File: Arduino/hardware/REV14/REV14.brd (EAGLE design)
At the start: 100 x 50 mm, 57 parts, among them IC1 LTC3525, IC2 ATMEGA168-AU, IC3 TS1003IG5TMF, Q1 32768Hz, U1 RN2483, U2 TMP112

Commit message: rev 14 really ready now
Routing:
- net SCL: track 95.6 -> 90.3 mm
- net GND: vias 128 -> 131
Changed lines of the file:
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@@
 <via x="95.09" y="25.175" extent="1-16" drill="0.5"/>
 <via x="63.6575" y="29.62" extent="1-16" drill="0.5"/>
+<via x="24.2875" y="29.62" extent="1-16" drill="0.5"/>
+<via x="29.3675" y="23.27" extent="1-16" drill="0.5"/>
+<via x="31.59" y="13.745" extent="1-16" drill="0.5"/>
 </signal>
 <signal name="VCC" class="1">
@@
 <wire x1="57.39" y1="31.75" x2="55.88" y2="31.75" width="0.2032" layer="1"/>
 <wire x1="55.88" y1="31.75" x2="55.88" y2="28.125" width="0.2032" layer="1"/>
-<wire x1="55.88" y1="28.125" x2="55.88" y2="27.7175" width="0.2032" layer="1"/>
-<wire x1="55.88" y1="27.7175" x2="57.88" y2="25.7175" width="0.2032" layer="1" curve="90"/>
-<wire x1="57.88" y1="25.7175" x2="60.0075" y2="25.7175" width="0.2032" layer="1"/>
 <wire x1="57.42" y1="31.78" x2="57.42" y2="32.4325" width="0.2032" layer="1"/>
 <wire x1="57.42" y1="32.4325" x2="57.15" y2="32.7025" width="0.2032" layer="1" curve="90"/>
@@
 <contactref element="TP1" pad="TP"/>
 <wire x1="22.0025" y1="48.895" x2="18.7325" y2="45.9425" width="1.016" layer="1" curve="90"/>
-<wire x1="18.7325" y1="45.9425" x2="18.7325" y2="44.2275" width="1.016" layer="1"/>
+<wire x1="18.7325" y1="45.9425" x2="18.7325" y2="45.75" width="1.016" layer="1"/>
+<wire x1="18.7325" y1="45.75" x2="18.7325" y2="45.72" width="1.016" layer="1"/>
+<wire x1="18.7325" y1="45.72" x2="18.7325" y2="44.2275" width="1.016" layer="1"/>
 <wire x1="18.7325" y1="44.2275" x2="18.5975" y2="44.2275" width="0.4064" layer="1"/>
 <wire x1="22.0025" y1="48.895" x2="93.000815625" y2="48.895" width="1.016" layer="1"/>
 <contactref element="PAD3" pad="1"/>
-<wire x1="18.7325" y1="45.9425" x2="18.7325" y2="45.72" width="0" layer="19" extent="1-1"/>
+<wire x1="18.75" y1="45.75" x2="18.7325" y2="45.72" width="2.1844" layer="1"/>
+<wire x1="18.75" y1="45.75" x2="18.7325" y2="45.75" width="2.1844" layer="1"/>
 </signal>
 <signal name="N$33" class="2">
@@
 <wire x1="2.635" y1="48.895" x2="4.985" y2="48.895" width="1.016" layer="1"/>
 <wire x1="4.985" y1="48.895" x2="6.985" y2="45.9425" width="1.016" layer="1" curve="-90"/>
-<wire x1="6.985" y1="45.9425" x2="6.985" y2="44.2275" width="1.016" layer="1"/>
+<wire x1="6.985" y1="45.9425" x2="6.985" y2="45.75" width="1.016" layer="1"/>
+<wire x1="6.985" y1="45.75" x2="6.985" y2="45.72" width="1.016" layer="1"/>
+<wire x1="6.985" y1="45.72" x2="6.985" y2="44.2275" width="1.016" layer="1"/>
 <wire x1="6.985" y1="44.2275" x2="7.1475" y2="44.2275" width="0.4064" layer="1"/>
 <wire x1="2.9525" y1="0.97" x2="0.97" y2="2.9525" width="1.016" layer="1" curve="-90"/>
@@
 <contactref element="TP4" pad="TP"/>
 <wire x1="92.71" y1="0.97" x2="2.9525" y2="0.97" width="1.016" layer="1"/>
-<wire x1="6.985" y1="45.9425" x2="6.985" y2="45.72" width="0" layer="19" extent="1-1"/>
+<wire x1="7" y1="45.75" x2="6.985" y2="45.72" width="2.1844" layer="1"/>
+<wire x1="7" y1="45.75" x2="6.985" y2="45.75" width="2.1844" layer="1"/>
 </signal>
 <signal name="N$2">

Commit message: rev14 without blooper
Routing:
- net SCL: track 90.3 -> 88.7 mm
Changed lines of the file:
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@@
 <contactref element="FTDI_RN2483" pad="1"/>
 <via x="61.055" y="38.325" extent="1-16" drill="0.5"/>
-<wire x1="58.6025" y1="38.29" x2="61.055" y2="38.29" width="0.4064" layer="1"/>
+<wire x1="58.6025" y1="38.29" x2="61.055" y2="38.29" width="0.3048" layer="1"/>
 <wire x1="61.055" y1="38.29" x2="61.055" y2="38.325" width="0.4064" layer="1"/>
 <via x="58.1" y="34.515" extent="1-16" drill="0.5"/>
-<wire x1="58.1025" y1="36.64" x2="58.1" y2="36.64" width="0.4064" layer="1"/>
-<wire x1="58.1" y1="36.64" x2="58.1" y2="34.515" width="0.4064" layer="1"/>
+<wire x1="58.1025" y1="36.64" x2="58.1" y2="36.64" width="0.3048" layer="1"/>
+<wire x1="58.1" y1="36.64" x2="58.1" y2="34.515" width="0.3048" layer="1"/>
 <via x="38.5" y="24.765" extent="1-16" drill="0.5"/>
 <via x="39.935" y="28.8925" extent="1-16" drill="0.5"/>
@@
 <wire x1="57.365" y1="43.815" x2="57.5167125" y2="43.6632875" width="0.4064" layer="1"/>
 <wire x1="57.5167125" y1="43.6632875" x2="58.1025" y2="42.249071875" width="0.4064" layer="1" curve="-45.00009"/>
-<wire x1="58.1025" y1="42.249071875" x2="58.1025" y2="38.29" width="0.4064" layer="1"/>
+<wire x1="58.1025" y1="42.249071875" x2="58.1025" y2="38.29" width="0.3048" layer="1"/>
 <wire x1="54.2925" y1="38.315" x2="53.9257875" y2="38.6817125" width="0.4064" layer="1"/>
 <wire x1="53.9257875" y1="38.6817125" x2="53.34" y2="40.095928125" width="0.4064" layer="1" curve="-45.00009"/>
@@
 <contactref element="I2C_EXT" pad="11"/>
 <contactref element="U2" pad="6"/>
-<wire x1="57.6025" y1="38.29" x2="55.88" y2="38.29" width="0.2032" layer="1"/>
-<wire x1="55.88" y1="38.29" x2="55.88" y2="39.2425" width="0.2032" layer="1"/>
+<wire x1="57.6025" y1="38.29" x2="55.75" y2="38.29" width="0.2032" layer="1"/>
+<wire x1="55.75" y1="38.29" x2="55.75" y2="39.2425" width="0.2032" layer="1"/>
 <contactref element="JP2" pad="1"/>
-<wire x1="55.88" y1="39.2425" x2="55.88" y2="43.6" width="0.2032" layer="1"/>
-<wire x1="55.88" y1="43.6" x2="55.665" y2="43.815" width="0.4064" layer="1" curve="90"/>
+<wire x1="55.75" y1="39.2425" x2="55.75" y2="43.6" width="0.2032" layer="1"/>
+<wire x1="55.75" y1="43.6" x2="55.665" y2="43.815" width="0.4064" layer="1" curve="90"/>
 <contactref element="U$4" pad="1"/>
 <wire x1="57.42" y1="29.18" x2="59.295" y2="27.305" width="0.2032" layer="1" curve="90"/>
@@
 <wire x1="57.42" y1="29.18" x2="57.42" y2="27.575" width="0.2032" layer="1"/>
 <wire x1="57.42" y1="27.575" x2="57.15" y2="27.305" width="0.2032" layer="1" curve="-90"/>
-<wire x1="57.15" y1="27.305" x2="55.88" y2="27.305" width="0.2032" layer="16"/>
-<wire x1="55.88" y1="27.305" x2="55.88" y2="39.2425" width="0.2032" layer="16"/>
+<wire x1="57.15" y1="27.305" x2="55.75" y2="27.305" width="0.2032" layer="16"/>
+<wire x1="55.75" y1="27.305" x2="55.75" y2="39.2425" width="0.2032" layer="16"/>
 <via x="57.15" y="27.305" extent="1-16" drill="0.5"/>
-<via x="55.88" y="39.2425" extent="1-16" drill="0.5"/>
+<via x="55.75" y="39.2425" extent="1-16" drill="0.5"/>
 <wire x1="45" y1="25.375" x2="42.5" y2="25.375" width="0.2032" layer="1"/>
 <wire x1="46.375" y1="24" x2="45" y2="25.375" width="0.2032" layer="1"/>
@@
 <contactref element="I2C_EXT" pad="9"/>
 <contactref element="U2" pad="1"/>
-<wire x1="57.6025" y1="36.64" x2="56.515" y2="36.64" width="0.4064" layer="1"/>
+<wire x1="57.6025" y1="36.64" x2="56.515" y2="36.64" width="0.3048" layer="1"/>
 <contactref element="JP2" pad="2"/>
 <wire x1="56.515" y1="36.64" x2="55.88" y2="36.64" width="0.2032" layer="1"/>
 <wire x1="55.88" y1="36.64" x2="55.855" y2="36.615" width="0.2032" layer="1" curve="-90"/>
-<wire x1="55.855" y1="36.615" x2="55.7784" y2="36.615" width="0.2032" layer="1"/>
+<wire x1="55.855" y1="36.615" x2="55.75" y2="36.615" width="0.2032" layer="1"/>
 <contactref element="U$4" pad="6"/>
-<wire x1="55.7784" y1="36.615" x2="54.2925" y2="36.615" width="0.2032" layer="1"/>
+<wire x1="55.75" y1="36.615" x2="54.2925" y2="36.615" width="0.2032" layer="1"/>
 <wire x1="57.42" y1="31.78" x2="57.39" y2="31.75" width="0.4064" layer="1" curve="-90"/>
 <wire x1="57.39" y1="31.75" x2="55.88" y2="31.75" width="0.2032" layer="1"/>
@@
 <wire x1="86.25" y1="7.25" x2="86.36" y2="7.175" width="0.2032" layer="16"/>
 <wire x1="67.125" y1="42.75" x2="69.125" y2="42.75" width="0.2032" layer="1"/>
-<wire x1="59.895" y1="35.52" x2="61.0063" y2="36.6313" width="0.2032" layer="1"/>
 <wire x1="61.0063" y1="36.6313" x2="67.125" y2="42.75" width="0.2032" layer="1"/>
 <wire x1="69.125" y1="42.75" x2="69.215" y2="42.8625" width="0.2032" layer="1"/>
@@
 <wire x1="60.2488" y1="37.3888" x2="61.0063" y2="36.6313" width="0.2032" layer="1"/>
 <wire x1="55.9816" y1="37.3888" x2="60.2488" y2="37.3888" width="0.2032" layer="1"/>
-<wire x1="55.7784" y1="37.1856" x2="55.9816" y2="37.3888" width="0.2032" layer="1"/>
-<wire x1="55.7784" y1="36.615" x2="55.7784" y2="37.1856" width="0.2032" layer="1"/>
+<wire x1="55.75" y1="37.1856" x2="55.9816" y2="37.3888" width="0.2032" layer="1"/>
+<wire x1="55.75" y1="36.615" x2="55.75" y2="37.1856" width="0.2032" layer="1"/>
 </signal>
 <signal name="RESET">

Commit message: rev14 pre routing.... again :-D
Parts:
- removed PAD2, PAD3: (no value), wirepad:3,81/1,4
- removed TP4: TPSQTP06R, testpad:TP06R
- added TP3: TPSQTP07R, testpad:TP07R
- moved R17 19.4 mm to (36.5, 12.4)
- moved FTDI_RN2483 19.4 mm to (31.1, 7.30)
- moved R7 19.4 mm to (29.8, 11.1)
- moved C11 14.9 mm to (20.6, 7.30), turned to 0 degrees
- moved R5 8.86 mm to (16.8, 9.53), turned to 0 degrees
- moved PHT 8.03 mm to (44.5, 14.0)
- moved R1 8.03 mm to (43.2, 8.89)
- moved C5 3.19 mm to (94.3, 14.0)
- moved DQ 3.19 mm to (76.5, 13.3)
- moved R18 3.19 mm to (87.3, 15.2)
- moved R3 3.19 mm to (82.2, 15.2)
- moved R4 3.19 mm to (84.8, 15.2)
- moved R9 3.19 mm to (79.7, 15.2)
- moved I2C_EXT 3.19 mm to (85.4, 9.08)
- moved C3 2.25 mm to (97.5, 30.8)
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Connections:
- net N$22: no longer PAD3.1
- net N$33: now also TP3.TP; no longer PAD2.1, TP4.TP
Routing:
- net VCC: track 231.3 -> 96.8 mm
- net SPI_MOSI: track 90.1 -> 0.00 mm, vias 2 -> 0
- net PHONE: track 83.0 -> 0.00 mm, vias 5 -> 0
- net SPI_MISO: track 81.9 -> 0.00 mm, vias 3 -> 0
- net RFM_IRQ: track 74.2 -> 0.00 mm, vias 2 -> 0
- net SCL: track 88.7 -> 19.2 mm, vias 4 -> 2
- net SDA: track 95.8 -> 26.3 mm, vias 5 -> 2
- net SPI_SCK: track 66.7 -> 0.00 mm, vias 3 -> 0
- net RESET: track 66.7 -> 3.11 mm, vias 2 -> 0
- net D2: track 61.7 -> 0.00 mm
- net VCC1: track 63.1 -> 2.53 mm
- net IO_POWER_UP: track 60.3 -> 0.00 mm, vias 1 -> 0
- net SPI_NSS: track 55.9 -> 0.00 mm, vias 3 -> 0
- net TX: track 49.9 -> 0.00 mm, vias 2 -> 0
- net RX: track 46.5 -> 0.00 mm, vias 2 -> 0
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
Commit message: rev14 routed again
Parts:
- added PAD2, PAD3: (no value), wirepad:3,81/1,4
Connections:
- net N$22: now also PAD2.1
- net N$33: now also PAD3.1
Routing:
- net VCC: track 96.8 -> 236.5 mm, vias 1 -> 8
- net SPI_MISO: track 0.00 -> 83.3 mm, vias 0 -> 2
- net SPI_MOSI: track 0.00 -> 83.0 mm, vias 0 -> 2
- net PHONE: track 0.00 -> 78.2 mm, vias 0 -> 4
- net SCL: track 19.2 -> 90.0 mm, vias 2 -> 5
- net SPI_SCK: track 0.00 -> 70.6 mm, vias 0 -> 2
- net RFM_IRQ: track 0.00 -> 67.5 mm, vias 0 -> 3
- net RESET: track 3.11 -> 69.0 mm, vias 0 -> 3
- net SDA: track 26.3 -> 88.4 mm, vias 2 -> 6
- net VCC1: track 2.53 -> 64.1 mm, vias 0 -> 1
- net D2: track 0.00 -> 56.1 mm, vias 0 -> 2
- net SPI_NSS: track 0.00 -> 54.2 mm, vias 0 -> 3
- net IO_POWER_UP: track 0.00 -> 52.3 mm, vias 0 -> 2
- net TX: track 0.00 -> 50.9 mm, vias 0 -> 2
- net RX: track 0.00 -> 45.7 mm, vias 0 -> 4
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
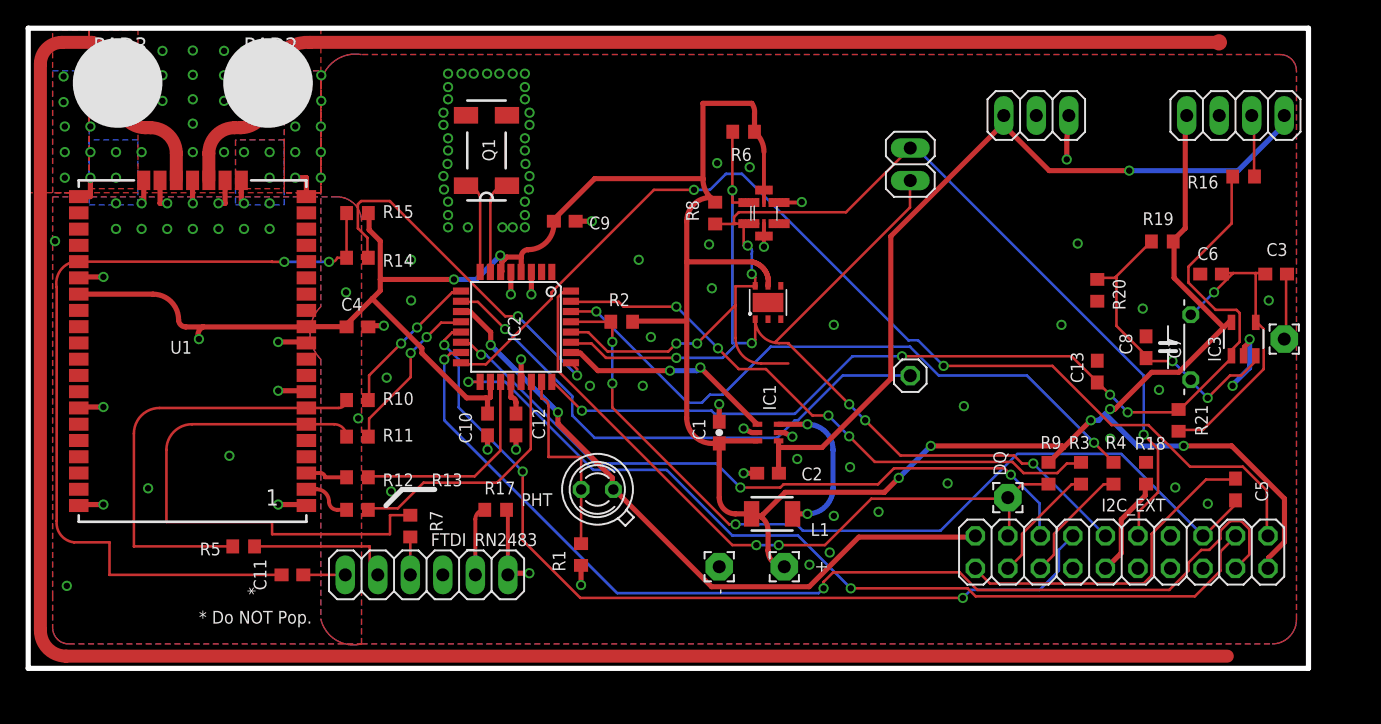
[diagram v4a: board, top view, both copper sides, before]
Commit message: rev14 ground plane fixed
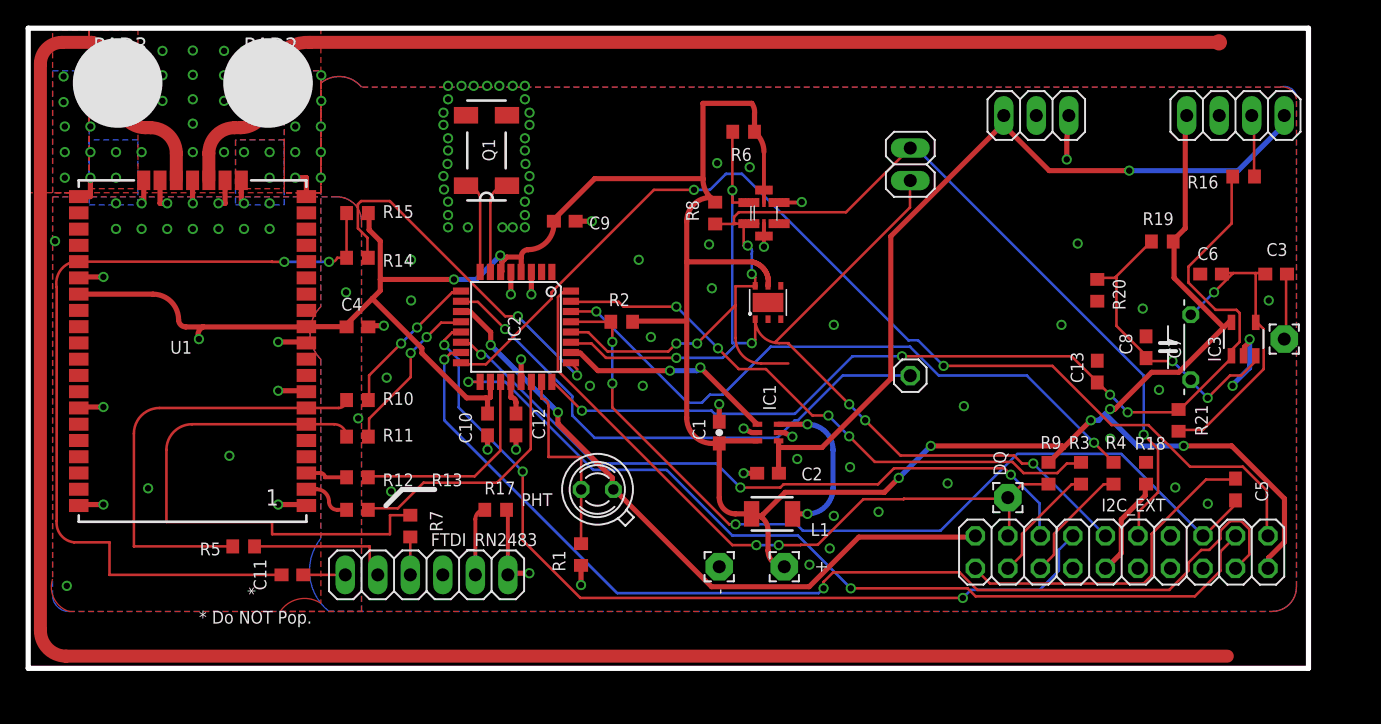
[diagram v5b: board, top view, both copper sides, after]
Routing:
- net GND: vias 143 -> 141
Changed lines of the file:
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@@
 <via x="22.8575" y="40.3225" extent="1-16" drill="0.5"/>
 <via x="22.8575" y="38.3225" extent="1-16" drill="0.5"/>
-<via x="32.795" y="46.45" extent="1-16" drill="0.5"/>
-<via x="34.795" y="46.45" extent="1-16" drill="0.5"/>
-<via x="38.795" y="46.45" extent="1-16" drill="0.5"/>
-<via x="36.795" y="46.45" extent="1-16" drill="0.5"/>
+<via x="32.795" y="45.4975" extent="1-16" drill="0.5"/>
+<via x="34.795" y="45.4975" extent="1-16" drill="0.5"/>
+<via x="38.795" y="45.4975" extent="1-16" drill="0.5"/>
+<via x="36.795" y="45.4975" extent="1-16" drill="0.5"/>
 <via x="32.795" y="34.45" extent="1-16" drill="0.5"/>
 <via x="34.34" y="34.45" extent="1-16" drill="0.5"/>
@@
 <via x="38.84" y="39.4025" extent="1-16" drill="0.5"/>
 <via x="38.795" y="41.4025" extent="1-16" drill="0.5"/>
-<via x="38.795" y="45.4025" extent="1-16" drill="0.5"/>
 <via x="39.1575" y="43.4025" extent="1-16" drill="0.5"/>
 <via x="39.1125" y="37.4025" extent="1-16" drill="0.5"/>
@@
 <via x="32.75" y="39.4025" extent="1-16" drill="0.5"/>
 <via x="32.795" y="41.4025" extent="1-16" drill="0.5"/>
-<via x="32.795" y="45.4025" extent="1-16" drill="0.5"/>
 <via x="32.4325" y="43.4025" extent="1-16" drill="0.5"/>
 <via x="32.4775" y="37.4025" extent="1-16" drill="0.5"/>
-<via x="33.8425" y="46.45" extent="1-16" drill="0.5"/>
-<via x="37.8425" y="46.45" extent="1-16" drill="0.5"/>
-<via x="35.8425" y="46.45" extent="1-16" drill="0.5"/>
+<via x="33.8425" y="45.4975" extent="1-16" drill="0.5"/>
+<via x="37.8425" y="45.4975" extent="1-16" drill="0.5"/>
+<via x="35.8425" y="45.4975" extent="1-16" drill="0.5"/>
 <via x="22.89" y="44.3225" extent="1-16" drill="0.5"/>
 <via x="22.89" y="46.3225" extent="1-16" drill="0.5"/>
@@
 <polygon width="0.3048" layer="1">
 <vertex x="22.86" y="24.13"/>
-<vertex x="22.86" y="3.81" curve="90"/>
-<vertex x="26.035" y="1.905"/>
-<vertex x="97.155" y="1.905" curve="90"/>
-<vertex x="99.06" y="3.81"/>
-<vertex x="99.06" y="46.6725" curve="90"/>
-<vertex x="97.79" y="47.9425"/>
-<vertex x="26.035" y="47.9425" curve="90"/>
+<vertex x="22.86" y="5.08" curve="90"/>
+<vertex x="19.685" y="4.445"/>
+<vertex x="97.155" y="4.445" curve="90"/>
+<vertex x="99.06" y="6.35"/>
+<vertex x="99.06" y="44.45" curve="90"/>
+<vertex x="97.79" y="45.4025"/>
+<vertex x="26.035" y="45.4025" curve="90"/>
 <vertex x="22.86" y="45.72"/>
 <vertex x="22.86" y="28.2575" curve="90"/>
@@
 <polygon width="0.3048" layer="16">
 <vertex x="22.86" y="24.13"/>
-<vertex x="22.86" y="3.81" curve="90"/>
-<vertex x="26.035" y="1.905"/>
-<vertex x="97.155" y="1.905" curve="90"/>
-<vertex x="99.06" y="3.81"/>
-<vertex x="99.06" y="46.6725" curve="90"/>
-<vertex x="97.79" y="47.9425"/>
-<vertex x="26.035" y="47.9425" curve="90"/>
+<vertex x="22.86" y="10.16" curve="90"/>
+<vertex x="23.495" y="4.445"/>
+<vertex x="97.155" y="4.445" curve="90"/>
+<vertex x="99.06" y="6.35"/>
+<vertex x="99.06" y="44.7675" curve="90"/>
+<vertex x="97.79" y="45.4025"/>
+<vertex x="26.035" y="45.4025" curve="90"/>
 <vertex x="22.86" y="45.72"/>
 <vertex x="22.86" y="28.2575" curve="90"/>
@@
 <vertex x="24.13" y="36.83"/>
 <vertex x="1.905" y="36.83"/>
-<vertex x="1.905" y="5.715"/>
-<vertex x="1.905" y="3.175" curve="90"/>
-<vertex x="3.175" y="1.905"/>
-<vertex x="26.035" y="1.905"/>
+<vertex x="1.905" y="6.985" curve="90"/>
+<vertex x="3.175" y="4.445"/>
+<vertex x="26.035" y="4.445"/>
 <vertex x="26.035" y="34.925" curve="90"/>
 </polygon>
@@
 <vertex x="24.13" y="36.83"/>
 <vertex x="1.905" y="36.83"/>
-<vertex x="1.905" y="5.715"/>
-<vertex x="1.905" y="3.175" curve="90"/>
-<vertex x="3.175" y="1.905"/>
-<vertex x="26.035" y="1.905"/>
+<vertex x="1.905" y="5.715" curve="90"/>
+<vertex x="3.175" y="4.445"/>
+<vertex x="26.035" y="4.445"/>
 <vertex x="26.035" y="34.925" curve="90"/>
 </polygon>
@@
 <via x="94.0725" y="22.0675" extent="1-16" drill="0.5"/>
 <via x="61.02" y="8.0975" extent="1-16" drill="0.5"/>
-<via x="62.6075" y="9.05" extent="1-16" drill="0.5"/>
+<via x="62.6075" y="9.3675" extent="1-16" drill="0.5"/>
 <via x="66.4175" y="12.225" extent="1-16" drill="0.5"/>
 <via x="64.195" y="15.7175" extent="1-16" drill="0.5"/>
@@
 <wire x1="56.875" y1="9.625" x2="55" y2="9.625" width="0.2032" layer="1"/>
 <wire x1="58.625" y1="9.625" x2="56.875" y2="9.625" width="0.2032" layer="16"/>
-<wire x1="62.23" y1="9.625" x2="58.625" y2="9.625" width="0.2032" layer="1"/>
-<wire x1="65.855" y1="13.25" x2="62.23" y2="9.625" width="0.2032" layer="1"/>
-<wire x1="76.5" y1="13.25" x2="65.855" y2="13.25" width="0.2032" layer="1"/>
+<wire x1="60.325" y1="9.625" x2="58.625" y2="9.625" width="0.2032" layer="1"/>
+<wire x1="76.5" y1="13.25" x2="68.395" y2="13.25" width="0.2032" layer="1"/>
 <wire x1="42.375" y1="29.375" x2="42.3926" y2="29.47" width="0.2032" layer="1"/>
 <wire x1="76.5" y1="13.25" x2="76.5175" y2="13.335" width="0.2032" layer="1"/>
@@
 <via x="56.875" y="9.625" extent="1-16" drill="0.5"/>
 <via x="58.625" y="9.625" extent="1-16" drill="0.5"/>
+<wire x1="65.2272" y1="13.208" x2="68.3768" y2="13.208" width="0.2032" layer="1"/>
+<wire x1="61.6712" y1="9.652" x2="65.2272" y2="13.208" width="0.2032" layer="1"/>
+<wire x1="60.3504" y1="9.652" x2="61.6712" y2="9.652" width="0.2032" layer="1"/>
+<wire x1="68.3768" y1="13.208" x2="68.395" y2="13.25" width="0.2032" layer="1"/>
+<wire x1="60.3504" y1="9.652" x2="60.325" y2="9.625" width="0.2032" layer="1"/>
 </signal>
 <signal name="IO_POWER_UP" class="1">
